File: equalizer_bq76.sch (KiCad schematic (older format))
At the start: 19 parts, among them J2 Conn_01x07_Female, U2 BQ76PL536A

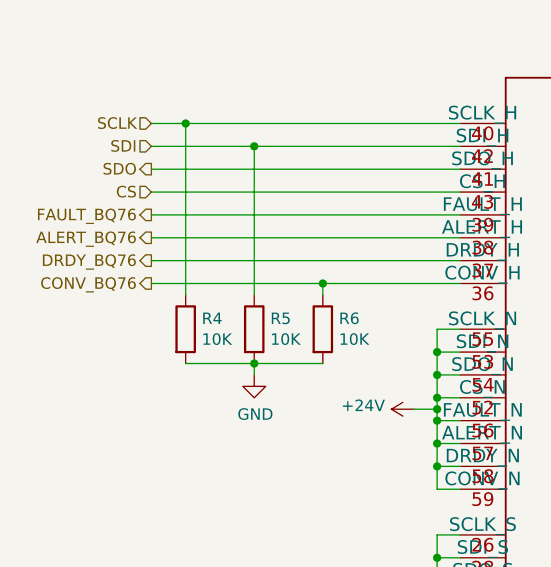
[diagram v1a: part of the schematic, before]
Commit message: Adds aux pins for bq76
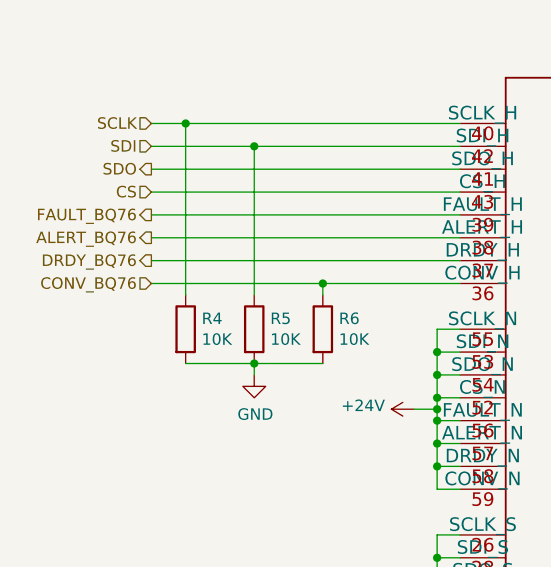
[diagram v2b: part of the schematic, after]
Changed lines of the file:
@@
 Wire Wire Line
 	3150 2450 1800 2450
-Text HLabel 1800 2550 0    50   Output ~ 0
+Text HLabel 1800 2550 0    50   Input ~ 0
 CONV_BQ76
 Wire Wire Line

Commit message: Dletes hw_balanceo folder
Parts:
- renumbered C17 to C2, C18 to C3, C19 to C4, C20 to C5, C21 to C6, C22 to C7, C23 to C8, C24 to C9, J2 to J1, R9 to R10, R10 to R11, R4 to R5, R5 to R6, R6 to R7, R7 to R8, R8 to R9
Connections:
- net GND: no longer C2.2, C3.2, C5.2, C6.2, C8.2, C9.2, J1.1 (Pin_1), R5.2, R6.2, R7.2, U2.13 (VC0), U2.14 (VSS), U2.15 (AGND), U2.21 (CONV_S), U2.22 (DRDY_S), U2.23 (ALERT_S), U2.24 (FAULT_S), U2.25 (VSSD), U2.26 (SCLK_S), U2.27 (SDO_S), U2.28 (SDI_S), U2.29 (CS_S), U2.33 (VSS), U2.34 (VSS), U2.35 (VSS), U2.49 (VSSD), U2.65 (PAD)
- net +24V renamed V_BAT
- new net GND_BAT: C2.2, C3.2, C5.2, C6.2, C8.2, C9.2, R5.2, R6.2, R7.2, U2.14 (VSS), U2.15 (AGND), U2.21 (CONV_S), U2.22 (DRDY_S), U2.23 (ALERT_S), U2.24 (FAULT_S), U2.25 (VSSD), U2.26 (SCLK_S), U2.27 (SDO_S), U2.28 (SDI_S), U2.29 (CS_S), U2.33 (VSS), U2.34 (VSS), U2.35 (VSS), U2.49 (VSSD), U2.65 (PAD)
- new net balancing_module/GND: J1.1 (Pin_1), U2.13 (VC0)

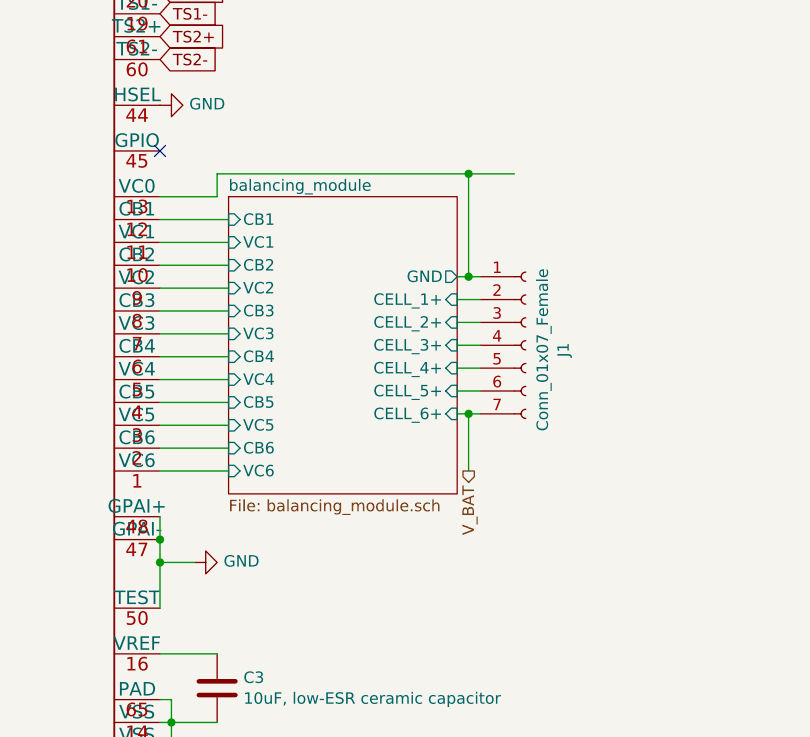
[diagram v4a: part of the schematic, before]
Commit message: Fixes missing footprints, adds initial pcb
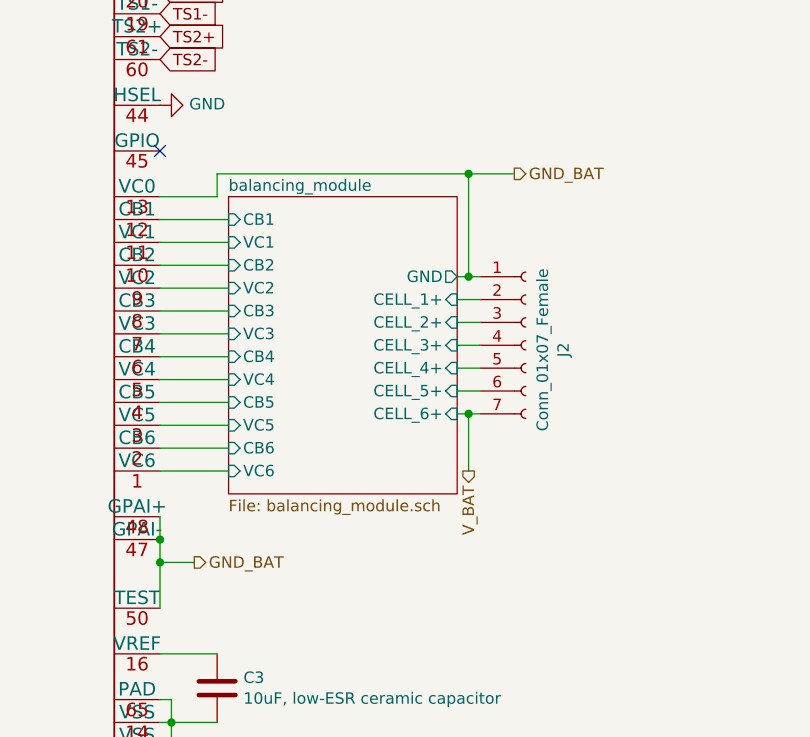
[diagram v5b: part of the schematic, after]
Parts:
- renumbered J1 to J2
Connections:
- net balancing_module/GND is gone; now on net GND_BAT: J2.1 (Pin_1), U2.13 (VC0)
- net GND: no longer U2.47 (GPAI-), U2.48 (GPAI+), U2.50 (TEST)
- net GND_BAT: now also U2.47 (GPAI-), U2.48 (GPAI+), U2.50 (TEST)
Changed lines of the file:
@@
 	2650 5000 3150 5000
 $Comp
-L power:GND #PWR016
+L power:GND #PWR018
 U 1 1 5FFB8D43
 P 4950 2350
-F 0 "#PWR016" H 4950 2100 50  0001 C CNN
+F 0 "#PWR018" H 4950 2100 50  0001 C CNN
 F 1 "GND" V 4955 2222 50  0000 R CNN
 F 2 "" H 4950 2350 50  0001 C CNN
@@
 Text Notes 9200 650  0    50   ~ 0
 LDO Cap. Filters
-$Comp
-L power:GND #PWR017
-U 1 1 6001D855
-P 5100 4350
-F 0 "#PWR017" H 5100 4100 50  0001 C CNN
-F 1 "GND" V 5105 4222 50  0000 R CNN
-F 2 "" H 5100 4350 50  0001 C CNN
-F 3 "" H 5100 4350 50  0001 C CNN
-	1    5100 4350
-	0    -1   -1   0
-$EndComp
 Wire Wire Line
 	4950 4550 4950 4350
@@
 Connection ~ 6300 2650
 $Comp
-L Connector:Conn_01x07_Female J1
+L Connector:Conn_01x07_Female J2
 U 1 1 5FF8226F
 P 6550 3400
-F 0 "J1" V 6715 3380 50  0000 C CNN
+F 0 "J2" V 6715 3380 50  0000 C CNN
 F 1 "Conn_01x07_Female" V 6624 3380 50  0000 C CNN
 F 2 "Connector_JST:JST_XH_S7B-XH-A_1x07_P2.50mm_Horizontal" H 6550 3400 50  0001 C CNN
@@
 Wire Wire Line
 	10200 1550 10400 1550
+Text HLabel 6500 2650 2    50   Output ~ 0
+GND_BAT
+Text HLabel 5100 4350 2    50   Output ~ 0
+GND_BAT
 $EndSCHEMATC

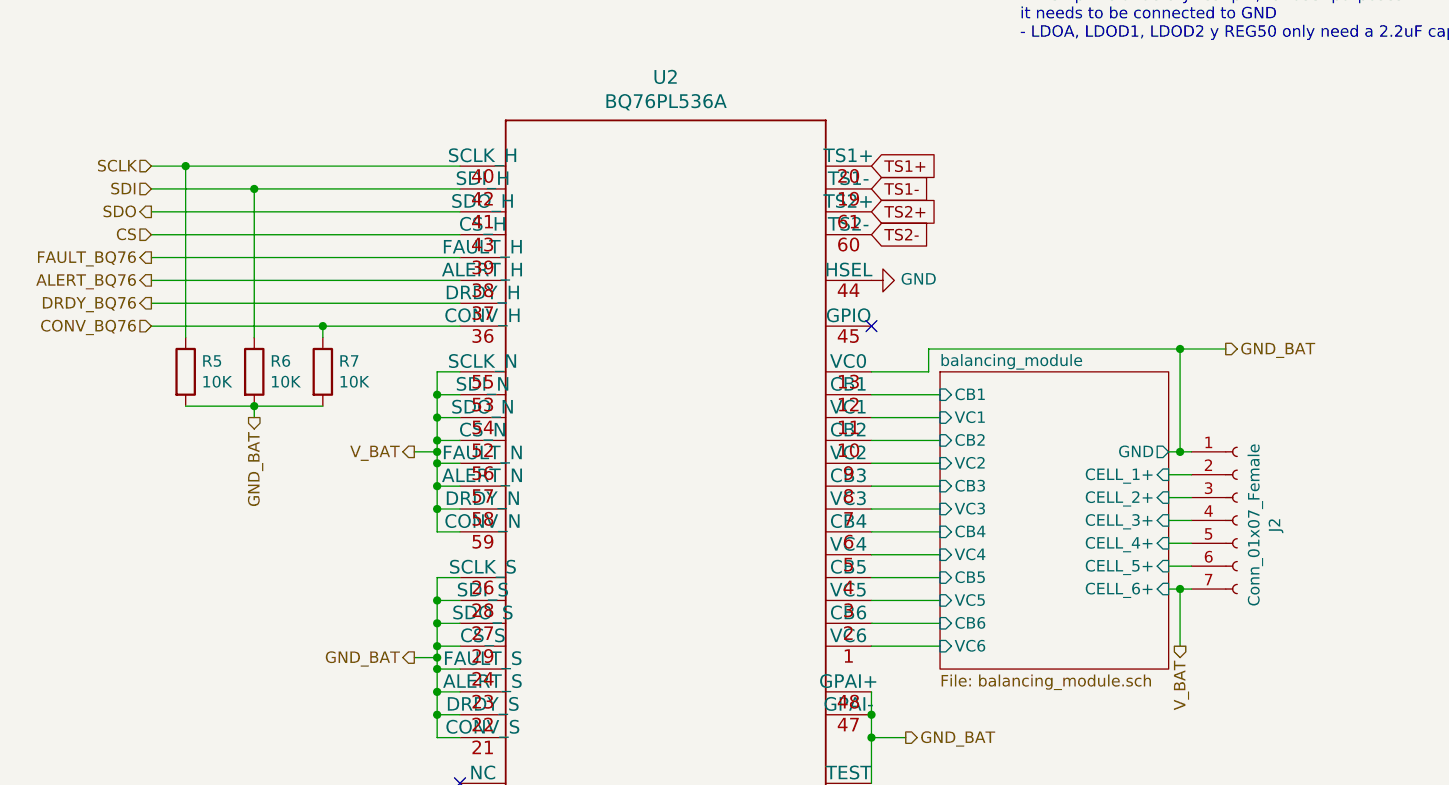
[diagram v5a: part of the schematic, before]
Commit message: add minor changes to schs
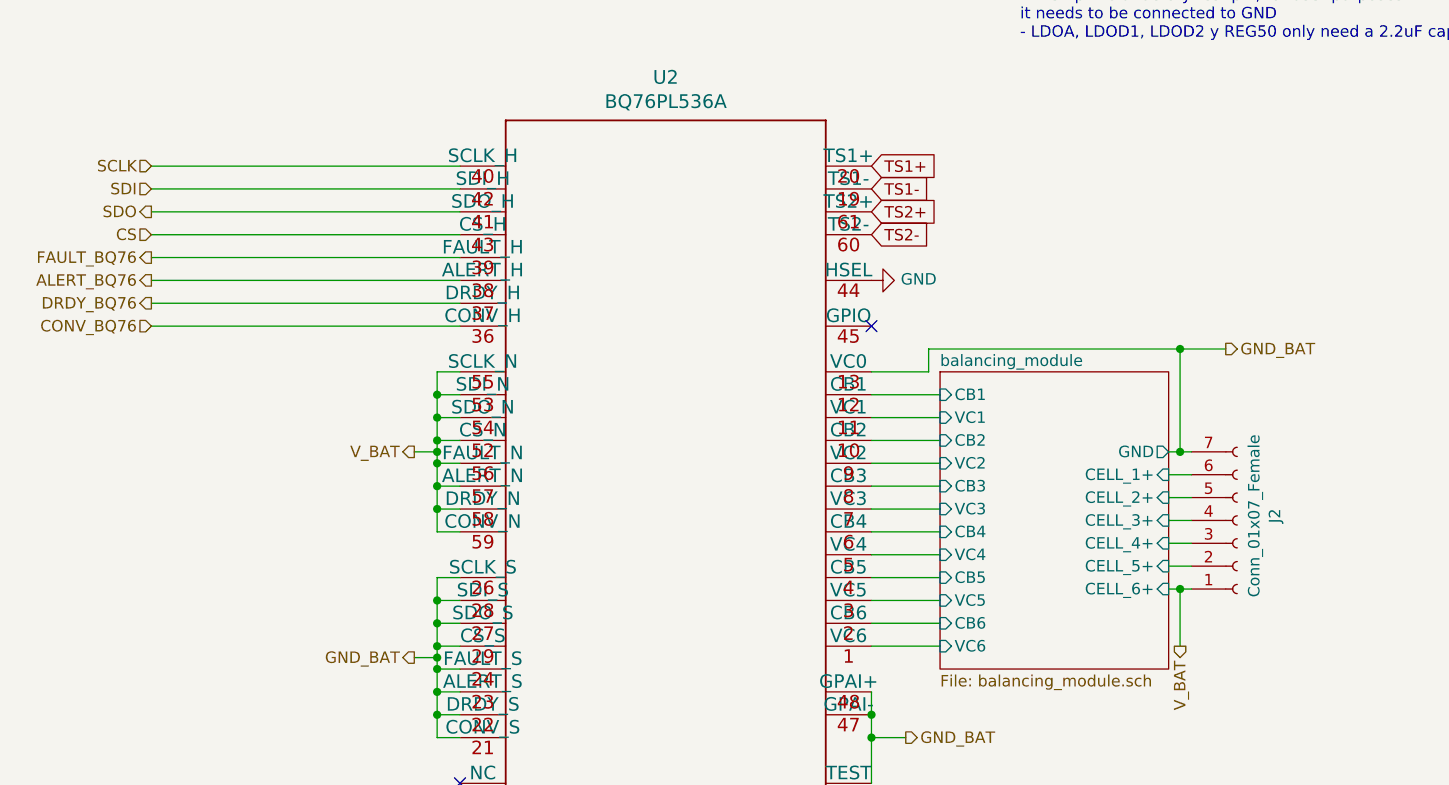
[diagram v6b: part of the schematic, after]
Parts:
- removed R5, R6, R7: 10K, Resistor_SMD:R_0805_2012Metric_Pad1.20x1.40mm_HandSolder, symbol Device:R
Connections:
- net GND_BAT: now also J2.7 (Pin_7); no longer J2.1 (Pin_1)
- net V_BAT: now also J2.1 (Pin_1); no longer J2.7 (Pin_7)
- net balancing_module/CELL_1+: now also J2.6 (Pin_6); no longer J2.2 (Pin_2)
- net balancing_module/CELL_2+: now also J2.5 (Pin_5); no longer J2.3 (Pin_3)
- net balancing_module/CELL_4+: now also J2.3 (Pin_3); no longer J2.5 (Pin_5)
- net balancing_module/CELL_5+: now also J2.2 (Pin_2); no longer J2.6 (Pin_6)
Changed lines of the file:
@@
 Text GLabel 9500 1050 1    50   Input ~ 0
 LDOA
-$Comp
-L Device:R R5
-U 1 1 6003EECE
-P 1950 2750
-F 0 "R5" H 2020 2796 50  0000 L CNN
-F 1 "10K" H 2020 2705 50  0000 L CNN
-F 2 "Resistor_SMD:R_0805_2012Metric_Pad1.20x1.40mm_HandSolder" V 1880 2750 50  0001 C CNN
-F 3 "~" H 1950 2750 50  0001 C CNN
-	1    1950 2750
-	1    0    0    -1
-$EndComp
-$Comp
-L Device:R R6
-U 1 1 6003F38A
-P 2250 2750
-F 0 "R6" H 2320 2796 50  0000 L CNN
-F 1 "10K" H 2320 2705 50  0000 L CNN
-F 2 "Resistor_SMD:R_0805_2012Metric_Pad1.20x1.40mm_HandSolder" V 2180 2750 50  0001 C CNN
-F 3 "~" H 2250 2750 50  0001 C CNN
-	1    2250 2750
-	1    0    0    -1
-$EndComp
-$Comp
-L Device:R R7
-U 1 1 6003F59D
-P 2550 2750
-F 0 "R7" H 2620 2796 50  0000 L CNN
-F 1 "10K" H 2620 2705 50  0000 L CNN
-F 2 "Resistor_SMD:R_0805_2012Metric_Pad1.20x1.40mm_HandSolder" V 2480 2750 50  0001 C CNN
-F 3 "~" H 2550 2750 50  0001 C CNN
-	1    2550 2750
-	1    0    0    -1
-$EndComp
-Wire Wire Line
-	2550 2600 2550 2550
-Wire Wire Line
-	2550 2550 3150 2550
-Wire Wire Line
-	3150 1950 2250 1950
-Wire Wire Line
-	2250 1950 2250 2600
-Wire Wire Line
-	3150 1850 1950 1850
-Wire Wire Line
-	1950 1850 1950 2600
-Wire Wire Line
-	1950 2900 2250 2900
-Connection ~ 2250 2900
-Wire Wire Line
-	2250 2900 2550 2900
-Wire Wire Line
-	2250 2900 2250 2950
 Text HLabel 1800 1850 0    50   Input ~ 0
 SCLK
-Wire Wire Line
-	1950 1850 1800 1850
-Connection ~ 1950 1850
 Text HLabel 1800 1950 0    50   Input ~ 0
 SDI
-Wire Wire Line
-	1800 1950 2250 1950
-Connection ~ 2250 1950
 Text HLabel 1800 2050 0    50   Output ~ 0
 SDO
@@
 Text HLabel 1800 2550 0    50   Input ~ 0
 CONV_BQ76
-Wire Wire Line
-	2550 2550 1800 2550
-Connection ~ 2550 2550
 $Comp
 L Device:R R10
@@
 $EndSheet
 Connection ~ 6300 2650
+Wire Wire Line
+	6250 3100 6300 3100
+Wire Wire Line
+	6250 3200 6350 3200
+Wire Wire Line
+	6250 3300 6350 3300
+Wire Wire Line
+	6250 3400 6350 3400
+Wire Wire Line
+	6250 3500 6350 3500
+Wire Wire Line
+	6350 3600 6250 3600
+Wire Wire Line
+	6300 2650 6300 3100
+Connection ~ 6300 3100
+Wire Wire Line
+	6300 3100 6350 3100
+Wire Notes Line
+	11200 2000 11200 550
+Wire Notes Line
+	9200 550  11200 550
+Wire Notes Line
+	9200 2000 11200 2000
+Text HLabel 10200 1600 3    50   Output ~ 0
+GND_BAT
+Wire Wire Line
+	6300 2650 6500 2650
+Text HLabel 2950 4000 0    50   Output ~ 0
+GND_BAT
+Text HLabel 6300 3950 3    50   Output ~ 0
+V_BAT
+Text HLabel 5000 5700 3    50   Output ~ 0
+GND_BAT
+Text HLabel 2650 5350 3    50   Output ~ 0
+GND_BAT
+Text HLabel 2350 5000 0    50   Output ~ 0
+V_BAT
+Wire Wire Line
+	6250 3700 6300 3700
+Wire Wire Line
+	6300 3950 6300 3700
+Connection ~ 6300 3700
+Wire Wire Line
+	6300 3700 6350 3700
+Wire Wire Line
+	9500 1550 9950 1550
+Connection ~ 9950 1550
+Wire Wire Line
+	9950 1550 10200 1550
+Connection ~ 10400 1550
+Wire Wire Line
+	10400 1550 10850 1550
+Wire Wire Line
+	10200 1550 10200 1600
+Connection ~ 10200 1550
+Wire Wire Line
+	10200 1550 10400 1550
+Text HLabel 6500 2650 2    50   Output ~ 0
+GND_BAT
+Text HLabel 5100 4350 2    50   Output ~ 0
+GND_BAT
 $Comp
 L Connector:Conn_01x07_Female J2
@@
 F 3 "~" H 6550 3400 50  0001 C CNN
 	1    6550 3400
-	1    0    0    -1
-$EndComp
-Wire Wire Line
-	6250 3100 6300 3100
-Wire Wire Line
-	6250 3200 6350 3200
-Wire Wire Line
-	6250 3300 6350 3300
-Wire Wire Line
-	6250 3400 6350 3400
-Wire Wire Line
-	6250 3500 6350 3500
-Wire Wire Line
-	6350 3600 6250 3600
-Wire Wire Line
-	6300 2650 6300 3100
-Connection ~ 6300 3100
-Wire Wire Line
-	6300 3100 6350 3100
-Wire Notes Line
-	11200 2000 11200 550
-Wire Notes Line
-	9200 550  11200 550
-Wire Notes Line
-	9200 2000 11200 2000
-Text HLabel 10200 1600 3    50   Output ~ 0
-GND_BAT
-Wire Wire Line
-	6300 2650 6500 2650
+	1    0    0    1
+$EndComp
+Wire Wire Line
+	1800 1850 3150 1850
+Wire Wire Line
+	1800 1950 3150 1950
+Wire Wire Line
+	1800 2550 3150 2550
 Text HLabel 2950 3100 0    50   Output ~ 0
 V_BAT
-Text HLabel 2950 4000 0    50   Output ~ 0
-GND_BAT
-Text HLabel 6300 3950 3    50   Output ~ 0
-V_BAT
-Text HLabel 5000 5700 3    50   Output ~ 0
-GND_BAT
-Text HLabel 2650 5350 3    50   Output ~ 0
-GND_BAT
-Text HLabel 2350 5000 0    50   Output ~ 0
-V_BAT
-Wire Wire Line
-	6250 3700 6300 3700
-Wire Wire Line
-	6300 3950 6300 3700
-Connection ~ 6300 3700
-Wire Wire Line
-	6300 3700 6350 3700
-Text HLabel 2250 2950 3    50   Output ~ 0
-GND_BAT
-Wire Wire Line
-	9500 1550 9950 1550
-Connection ~ 9950 1550
-Wire Wire Line
-	9950 1550 10200 1550
-Connection ~ 10400 1550
-Wire Wire Line
-	10400 1550 10850 1550
-Wire Wire Line
-	10200 1550 10200 1600
-Connection ~ 10200 1550
-Wire Wire Line
-	10200 1550 10400 1550
-Text HLabel 6500 2650 2    50   Output ~ 0
-GND_BAT
-Text HLabel 5100 4350 2    50   Output ~ 0
-GND_BAT
 $EndSCHEMATC

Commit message: Final version pcb
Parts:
- removed U2: BQ76PL536A, Package_QFP:HTQFP-64-1EP_10x10mm_P0.5mm_EP8x8mm, symbol bms_hardware-rescue:BQ76PL536A-Battery_Management
- added U2: BQ76PL536APAPR, Package_QFP:HTQFP-64-1EP_10x10mm_P0.5mm_EP8x8mm_Mask4.4x4.4mm_ThermalVias, symbol Battery_Management:BQ76PL536APAPR
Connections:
- net ALERT_BQ76: now also U2.38 (ALERT_H)
- net CONV_BQ76: now also U2.36 (CONV_H)
- net CS: now also U2.43 (CS_H)
- net DRDY_BQ76: now also U2.37 (DRDY_H)
- net FAULT_BQ76: now also U2.39 (FAULT_H)
- net GND: now also U2.44 (HSEL)
- net GND_BAT: now also U2.13 (VC0), U2.14 (VSS), U2.15 (AGND), U2.21 (CONV_S), U2.22 (DRDY_S), U2.23 (ALERT_S), U2.24 (FAULT_S), U2.25 (VSSD), U2.26 (SCLK_S), U2.27 (SDO_S), U2.28 (SDI_S), U2.29 (CS_S), U2.33 (VSS), U2.34 (VSS), U2.35 (VSS), U2.49 (VSSD), U2.50 (TEST), U2.65 (PAD)
- net LDOA: now also U2.17 (LDOA)
- net LDOD1: now also U2.18 (LDOD1)
- net LDOD2: now also U2.46 (LDOD2)
- net REG50: now also U2.32 (REG50)
- net SCLK: now also U2.40 (SCLK_H)
- net SDI: now also U2.42 (SDI_H)
- net SDO: now also U2.41 (SDO_H)
- net TS1+: now also U2.20 (TS1+)
- net TS1-: now also U2.19 (TS1-)
- net TS2+: now also U2.61 (TS2+)
- net TS2-: now also U2.60 (TS2-)
- net V_BAT: now also U2.52 (CS_N), U2.53 (SDI_N), U2.54 (SDO_N), U2.55 (SCLK_N), U2.56 (FAULT_N), U2.57 (ALERT_N), U2.58 (DRDY_N), U2.59 (CONV_N), U2.63 (BAT1), U2.64 (BAT2)
- net balancing_module/CB1: now also U2.12 (CB1)
- net balancing_module/CB2: now also U2.10 (CB2)
- net balancing_module/CB3: now also U2.8 (CB3)
- net balancing_module/CB4: now also U2.6 (CB4)
- net balancing_module/CB5: now also U2.4 (CB5)
- net balancing_module/CB6: now also U2.2 (CB6)
- net balancing_module/VC1: now also U2.11 (VC1)
- net balancing_module/VC2: now also U2.9 (VC2)
- net balancing_module/VC3: now also U2.7 (VC3)
- net balancing_module/VC4: now also U2.5 (VC4)
- net balancing_module/VC5: now also U2.3 (VC5)
- net balancing_module/VC6: now also U2.1 (VC6)
- net at C3.1: now also U2.16 (VREF)
- new net: U2.47 (GPAI-), U2.48 (GPAI+)
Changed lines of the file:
@@
 $Descr A4 11693 8268
 encoding utf-8
-Sheet 3 8
+Sheet 3 9
 Title ""
 Date ""
@@
 Wire Wire Line
 	4950 4350 5100 4350
-Connection ~ 4950 4350
 Text Notes 5600 750  0    50   ~ 10
 NOTES
@@
 Text GLabel 3150 5650 0    50   Input ~ 0
 REG50
-Wire Wire Line
-	4950 4350 4950 4250
-Wire Wire Line
-	4950 4150 4950 4250
-Connection ~ 4950 4250
-$Comp
-L bms_hardware-rescue:BQ76PL536A-Battery_Management U?
-U 1 1 5FE7709D
-P 4050 3750
-AR Path="/5FE7709D" Ref="U?"  Part="1"
-AR Path="/5FE7678E/5FE7709D" Ref="U2"  Part="1"
-F 0 "U2" H 4050 6038 60  0000 C CNN
-F 1 "BQ76PL536A" H 4050 5932 60  0000 C CNN
-F 2 "Package_QFP:HTQFP-64-1EP_10x10mm_P0.5mm_EP8x8mm" H 4050 3690 60  0001 C CNN
-F 3 "https://ar.mouser.com/ProductDetail/Texas-Instruments/BQ76PL536APAPT/?qs=UlfnwZ2x8nT1EXA%252BD%252BEfIQ%3D%3D" H 4050 5932 60  0001 C CNN
-	1    4050 3750
-	1    0    0    -1
-$EndComp
 Text GLabel 10850 1050 1    50   Input ~ 0
 REG50
@@
 Text HLabel 2950 3100 0    50   Output ~ 0
 V_BAT
+Wire Wire Line
+	4950 4150 4950 4250
+$Comp
+L Battery_Management:BQ76PL536APAPR U2
+U 1 1 603E20E4
+P 4050 3750
+F 0 "U2" H 4050 6038 60  0000 C CNN
+F 1 "BQ76PL536APAPR" H 4050 5932 60  0000 C CNN
+F 2 "Package_QFP:HTQFP-64-1EP_10x10mm_P0.5mm_EP8x8mm_Mask4.4x4.4mm_ThermalVias" H 4050 3690 60  0001 C CNN
+F 3 "" H 4050 3750 60  0000 C CNN
+	1    4050 3750
+	1    0    0    -1
+$EndComp
 $EndSCHEMATC
